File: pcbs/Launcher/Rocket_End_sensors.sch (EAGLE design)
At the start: 7 parts, among them U1 ARDUINO-MEGAPRO-5V, X1 22-23-2051, X3 22-23-2041, X5 22-23-2101, X6 22-23-2101

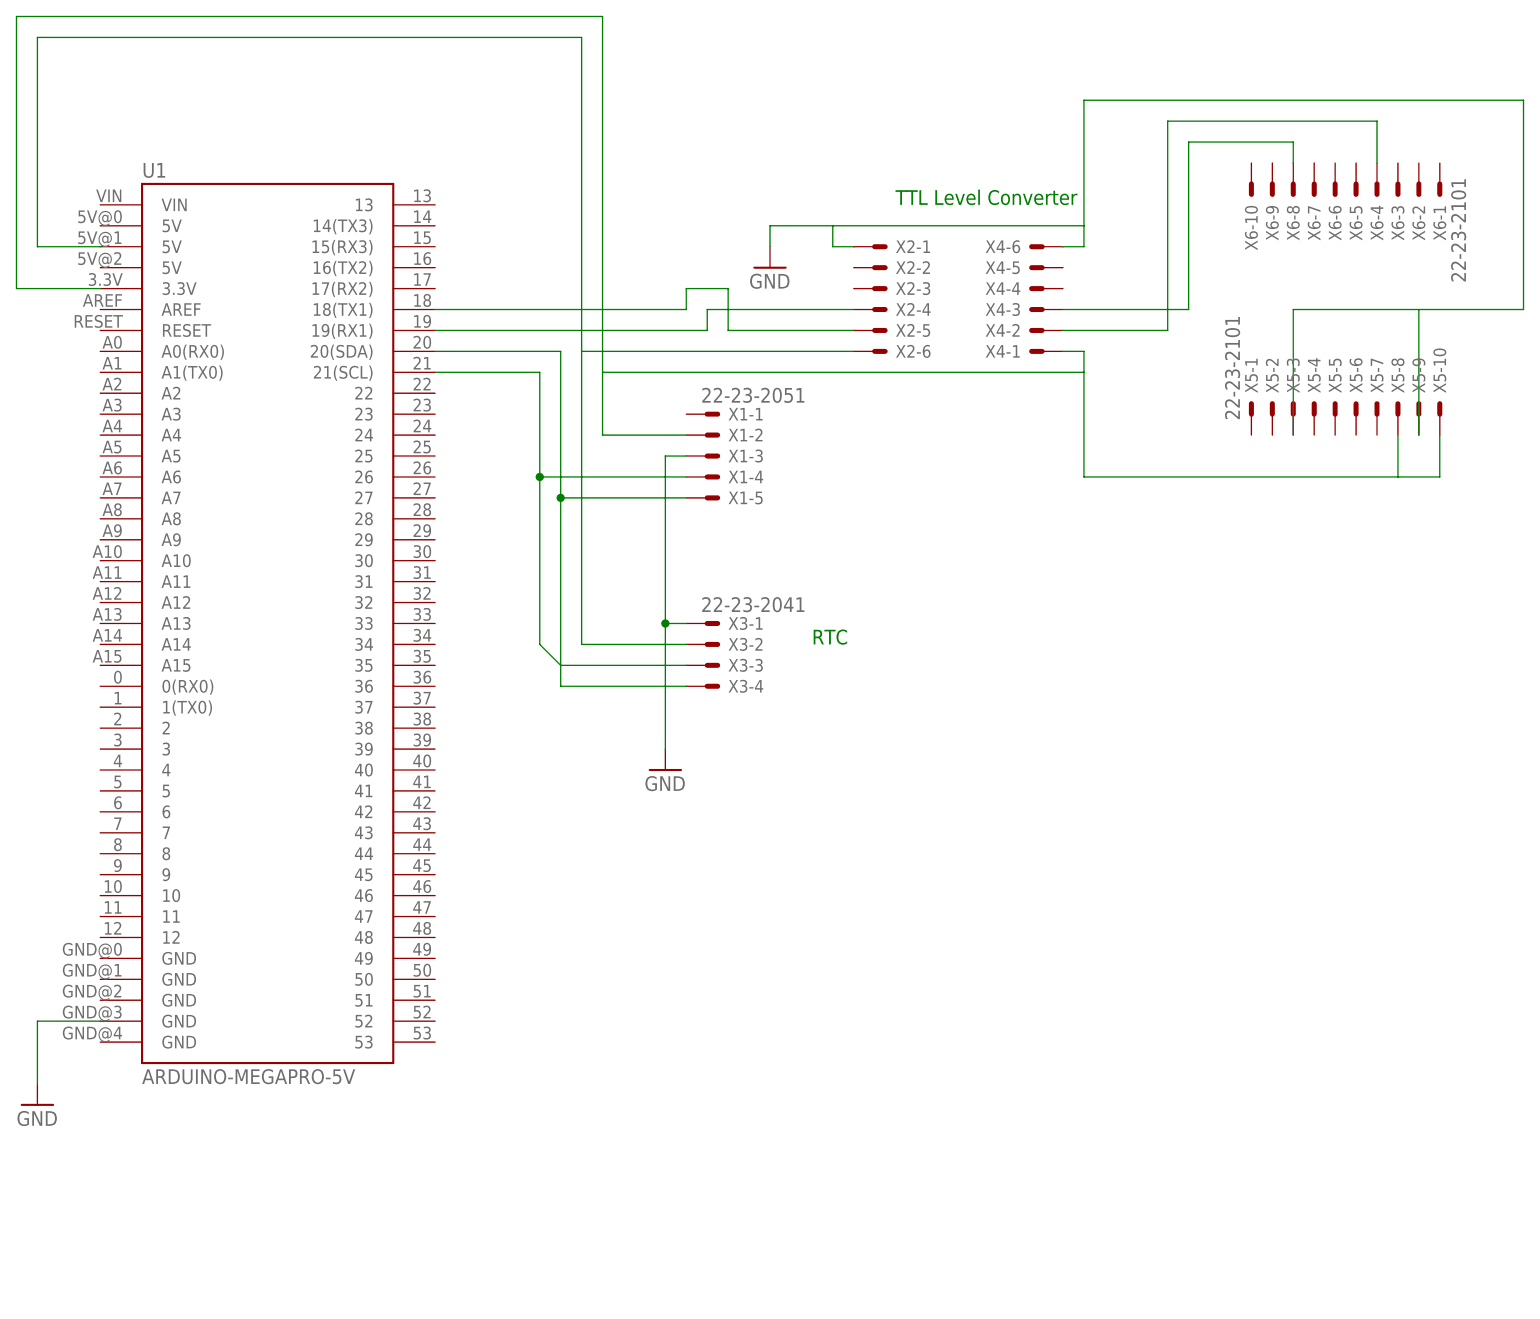
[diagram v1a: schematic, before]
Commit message: * Much better placement of components and tracks for Rocket_End * Put IMU on bottom of the Sensor board
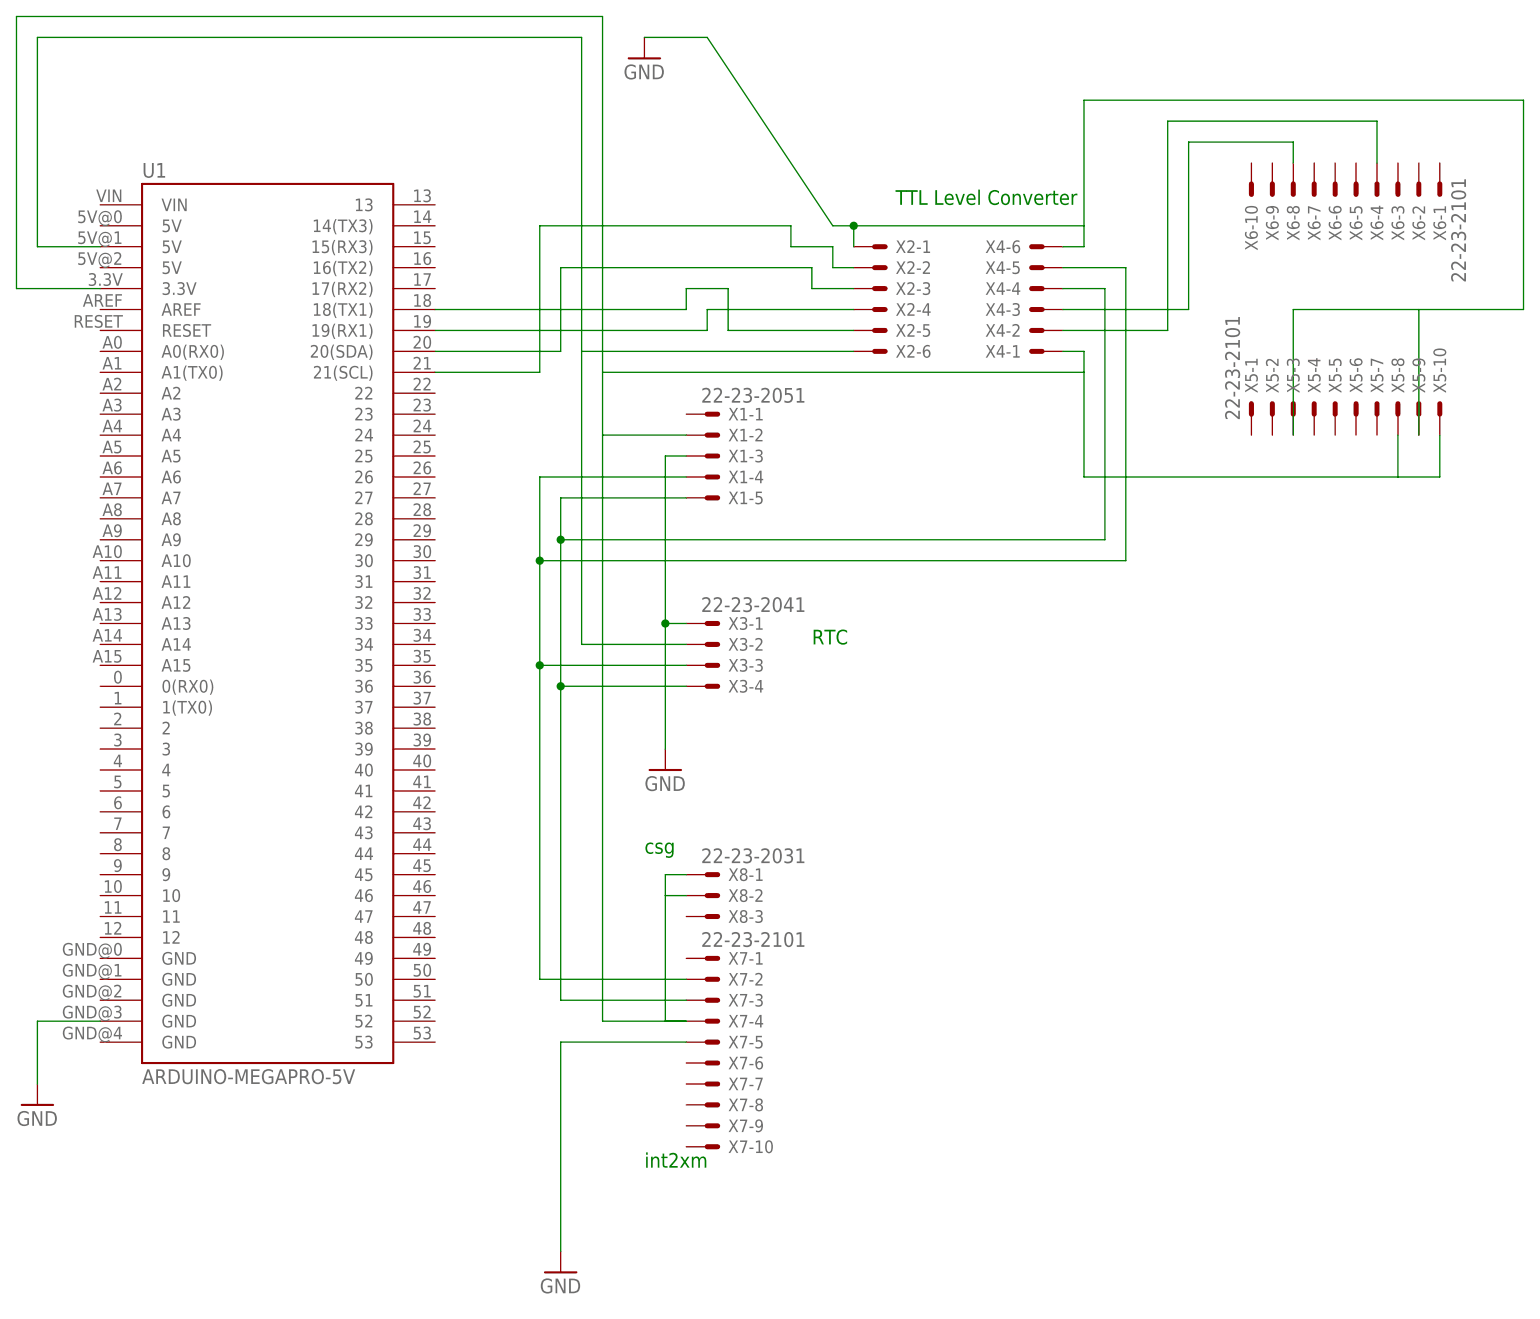
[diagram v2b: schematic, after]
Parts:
- added X7: 22-23-2101, con-molex:22-23-2101
- added X8: 22-23-2031, con-molex:22-23-2031
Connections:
- new net N$2: U1.21(SCL), X2-2.S
- new net N$5: U1.20(SDA), X2-3.S
- new net N$7: X2-1.S, X4-6.S, X5-3.S, X5-9.S
- net GND: now also X7-5.S; no longer X2-1.S, X4-6.S, X5-3.S, X5-9.S
- net N$18: now also X4-4.S, X7-3.S; no longer U1.20(SDA)
- net N$24: now also X4-5.S, X7-2.S; no longer U1.21(SCL)
- net N$4: now also X7-4.S, X8-1.S, X8-2.S
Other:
- note added: "csg"
- note added: "int2xm"
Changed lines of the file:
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@@
 <part name="X5" library="con-molex" deviceset="22-23-2101" device=""/>
 <part name="X6" library="con-molex" deviceset="22-23-2101" device=""/>
+<part name="X7" library="con-molex" deviceset="22-23-2101" device=""/>
+<part name="X8" library="con-molex" deviceset="22-23-2031" device=""/>
+<part name="GND3" library="supply1" deviceset="GND" device=""/>
 </parts>
 <sheets>
@@
 <text x="104.14" y="50.8" size="1.778" layer="91">RTC</text>
 <text x="114.3" y="104.14" size="1.778" layer="91">TTL Level Converter</text>
+<text x="83.82" y="-12.7" size="1.778" layer="91">int2xm</text>
+<text x="83.82" y="25.4" size="1.778" layer="91">csg</text>
 </plain>
 <instances>
@@
 <instance part="X4" gate="-5" x="132.08" y="96.52" rot="R180"/>
 <instance part="X4" gate="-6" x="132.08" y="99.06" rot="R180"/>
-<instance part="GND2" gate="1" x="99.06" y="96.52"/>
+<instance part="GND2" gate="1" x="83.82" y="121.92"/>
 <instance part="X5" gate="-1" x="157.48" y="78.74" rot="R90"/>
 <instance part="X5" gate="-2" x="160.02" y="78.74" rot="R90"/>
@@
 <instance part="X6" gate="-9" x="160.02" y="106.68" rot="R270"/>
 <instance part="X6" gate="-10" x="157.48" y="106.68" rot="R270"/>
+<instance part="X7" gate="-1" x="91.44" y="12.7"/>
+<instance part="X7" gate="-2" x="91.44" y="10.16"/>
+<instance part="X7" gate="-3" x="91.44" y="7.62"/>
+<instance part="X7" gate="-4" x="91.44" y="5.08"/>
+<instance part="X7" gate="-5" x="91.44" y="2.54"/>
+<instance part="X7" gate="-6" x="91.44" y="0"/>
+<instance part="X7" gate="-7" x="91.44" y="-2.54"/>
+<instance part="X7" gate="-8" x="91.44" y="-5.08"/>
+<instance part="X7" gate="-9" x="91.44" y="-7.62"/>
+<instance part="X7" gate="-10" x="91.44" y="-10.16"/>
+<instance part="X8" gate="-1" x="91.44" y="22.86"/>
+<instance part="X8" gate="-2" x="91.44" y="20.32"/>
+<instance part="X8" gate="-3" x="91.44" y="17.78"/>
+<instance part="GND3" gate="1" x="73.66" y="-25.4"/>
 </instances>
 <busses>
@@
 </segment>
 <segment>
-<pinref part="X4" gate="-6" pin="S"/>
-<wire x1="134.62" y1="99.06" x2="137.16" y2="99.06" width="0.1524" layer="91"/>
-<wire x1="137.16" y1="99.06" x2="137.16" y2="101.6" width="0.1524" layer="91"/>
-<wire x1="137.16" y1="101.6" x2="106.68" y2="101.6" width="0.1524" layer="91"/>
-<wire x1="106.68" y1="101.6" x2="106.68" y2="99.06" width="0.1524" layer="91"/>
-<pinref part="X2" gate="-1" pin="S"/>
-<wire x1="106.68" y1="99.06" x2="109.22" y2="99.06" width="0.1524" layer="91"/>
-<wire x1="106.68" y1="101.6" x2="99.06" y2="101.6" width="0.1524" layer="91"/>
-<wire x1="99.06" y1="101.6" x2="99.06" y2="99.06" width="0.1524" layer="91"/>
+<wire x1="106.68" y1="101.6" x2="91.44" y2="124.46" width="0.1524" layer="91"/>
+<wire x1="91.44" y1="124.46" x2="83.82" y2="124.46" width="0.1524" layer="91"/>
 <pinref part="GND2" gate="1" pin="GND"/>
-<pinref part="X5" gate="-9" pin="S"/>
-<wire x1="177.8" y1="76.2" x2="177.8" y2="91.44" width="0.1524" layer="91"/>
-<wire x1="177.8" y1="91.44" x2="162.56" y2="91.44" width="0.1524" layer="91"/>
-<pinref part="X5" gate="-3" pin="S"/>
-<wire x1="162.56" y1="91.44" x2="162.56" y2="76.2" width="0.1524" layer="91"/>
-<wire x1="177.8" y1="91.44" x2="190.5" y2="91.44" width="0.1524" layer="91"/>
-<wire x1="190.5" y1="91.44" x2="190.5" y2="116.84" width="0.1524" layer="91"/>
-<wire x1="190.5" y1="116.84" x2="137.16" y2="116.84" width="0.1524" layer="91"/>
-<wire x1="137.16" y1="116.84" x2="137.16" y2="101.6" width="0.1524" layer="91"/>
+</segment>
+<segment>
+<pinref part="X7" gate="-5" pin="S"/>
+<wire x1="88.9" y1="2.54" x2="73.66" y2="2.54" width="0.1524" layer="91"/>
+<wire x1="73.66" y1="2.54" x2="73.66" y2="-22.86" width="0.1524" layer="91"/>
+<pinref part="GND3" gate="1" pin="GND"/>
 </segment>
 </net>
 <net name="N$18" class="0">
 <segment>
-<pinref part="U1" gate="G$1" pin="20(SDA)"/>
-<wire x1="58.42" y1="86.36" x2="73.66" y2="86.36" width="0.1524" layer="91"/>
-<wire x1="73.66" y1="86.36" x2="73.66" y2="68.58" width="0.1524" layer="91"/>
-<pinref part="X3" gate="-4" pin="S"/>
-<wire x1="73.66" y1="68.58" x2="73.66" y2="45.72" width="0.1524" layer="91"/>
-<wire x1="73.66" y1="45.72" x2="88.9" y2="45.72" width="0.1524" layer="91"/>
+<wire x1="73.66" y1="68.58" x2="73.66" y2="63.5" width="0.1524" layer="91"/>
 <pinref part="X1" gate="-5" pin="S"/>
 <wire x1="88.9" y1="68.58" x2="73.66" y2="68.58" width="0.1524" layer="91"/>
-<junction x="73.66" y="68.58"/>
+<pinref part="X7" gate="-3" pin="S"/>
+<wire x1="73.66" y1="63.5" x2="73.66" y2="45.72" width="0.1524" layer="91"/>
+<wire x1="73.66" y1="45.72" x2="73.66" y2="7.62" width="0.1524" layer="91"/>
+<wire x1="73.66" y1="7.62" x2="88.9" y2="7.62" width="0.1524" layer="91"/>
+<wire x1="73.66" y1="63.5" x2="139.7" y2="63.5" width="0.1524" layer="91"/>
+<wire x1="139.7" y1="63.5" x2="139.7" y2="93.98" width="0.1524" layer="91"/>
+<pinref part="X4" gate="-4" pin="S"/>
+<wire x1="139.7" y1="93.98" x2="134.62" y2="93.98" width="0.1524" layer="91"/>
+<junction x="73.66" y="63.5"/>
+<pinref part="X3" gate="-4" pin="S"/>
+<wire x1="88.9" y1="45.72" x2="73.66" y2="45.72" width="0.1524" layer="91"/>
+<junction x="73.66" y="45.72"/>
 </segment>
 </net>
 <net name="N$24" class="0">
 <segment>
-<pinref part="U1" gate="G$1" pin="21(SCL)"/>
-<wire x1="58.42" y1="83.82" x2="71.12" y2="83.82" width="0.1524" layer="91"/>
-<wire x1="71.12" y1="83.82" x2="71.12" y2="71.12" width="0.1524" layer="91"/>
-<pinref part="X3" gate="-3" pin="S"/>
-<wire x1="71.12" y1="71.12" x2="71.12" y2="50.8" width="0.1524" layer="91"/>
-<wire x1="71.12" y1="50.8" x2="73.66" y2="48.26" width="0.1524" layer="91"/>
-<wire x1="73.66" y1="48.26" x2="88.9" y2="48.26" width="0.1524" layer="91"/>
+<wire x1="71.12" y1="71.12" x2="71.12" y2="60.96" width="0.1524" layer="91"/>
 <pinref part="X1" gate="-4" pin="S"/>
 <wire x1="88.9" y1="71.12" x2="71.12" y2="71.12" width="0.1524" layer="91"/>
-<junction x="71.12" y="71.12"/>
+<pinref part="X7" gate="-2" pin="S"/>
+<wire x1="71.12" y1="60.96" x2="71.12" y2="48.26" width="0.1524" layer="91"/>
+<wire x1="71.12" y1="48.26" x2="71.12" y2="10.16" width="0.1524" layer="91"/>
+<wire x1="71.12" y1="10.16" x2="88.9" y2="10.16" width="0.1524" layer="91"/>
+<pinref part="X4" gate="-5" pin="S"/>
+<wire x1="134.62" y1="96.52" x2="142.24" y2="96.52" width="0.1524" layer="91"/>
+<wire x1="142.24" y1="96.52" x2="142.24" y2="60.96" width="0.1524" layer="91"/>
+<wire x1="142.24" y1="60.96" x2="71.12" y2="60.96" width="0.1524" layer="91"/>
+<junction x="71.12" y="60.96"/>
+<pinref part="X3" gate="-3" pin="S"/>
+<wire x1="88.9" y1="48.26" x2="71.12" y2="48.26" width="0.1524" layer="91"/>
+<junction x="71.12" y="48.26"/>
 </segment>
 </net>
@@
 <wire x1="175.26" y1="71.12" x2="137.16" y2="71.12" width="0.1524" layer="91"/>
 <wire x1="137.16" y1="71.12" x2="137.16" y2="83.82" width="0.1524" layer="91"/>
+<wire x1="78.74" y1="76.2" x2="78.74" y2="5.08" width="0.1524" layer="91"/>
+<pinref part="X7" gate="-4" pin="S"/>
+<wire x1="78.74" y1="5.08" x2="88.9" y2="5.08" width="0.1524" layer="91"/>
+<wire x1="88.9" y1="5.08" x2="86.36" y2="5.08" width="0.1524" layer="91"/>
+<wire x1="86.36" y1="5.08" x2="86.36" y2="20.32" width="0.1524" layer="91"/>
+<pinref part="X8" gate="-1" pin="S"/>
+<wire x1="86.36" y1="20.32" x2="86.36" y2="22.86" width="0.1524" layer="91"/>
+<wire x1="86.36" y1="22.86" x2="88.9" y2="22.86" width="0.1524" layer="91"/>
+<pinref part="X8" gate="-2" pin="S"/>
+<wire x1="88.9" y1="20.32" x2="86.36" y2="20.32" width="0.1524" layer="91"/>
 </segment>
 </net>
@@
 </segment>
 </net>
+<net name="N$2" class="0">
+<segment>
+<pinref part="U1" gate="G$1" pin="21(SCL)"/>
+<wire x1="58.42" y1="83.82" x2="71.12" y2="83.82" width="0.1524" layer="91"/>
+<wire x1="71.12" y1="83.82" x2="71.12" y2="101.6" width="0.1524" layer="91"/>
+<wire x1="71.12" y1="101.6" x2="101.6" y2="101.6" width="0.1524" layer="91"/>
+<wire x1="101.6" y1="101.6" x2="101.6" y2="99.06" width="0.1524" layer="91"/>
+<wire x1="101.6" y1="99.06" x2="106.68" y2="99.06" width="0.1524" layer="91"/>
+<wire x1="106.68" y1="99.06" x2="106.68" y2="96.52" width="0.1524" layer="91"/>
+<pinref part="X2" gate="-2" pin="S"/>
+<wire x1="106.68" y1="96.52" x2="109.22" y2="96.52" width="0.1524" layer="91"/>
+</segment>
+</net>
+<net name="N$5" class="0">
+<segment>
+<pinref part="U1" gate="G$1" pin="20(SDA)"/>
+<wire x1="58.42" y1="86.36" x2="73.66" y2="86.36" width="0.1524" layer="91"/>
+<pinref part="X2" gate="-3" pin="S"/>
+<wire x1="109.22" y1="93.98" x2="104.14" y2="93.98" width="0.1524" layer="91"/>
+<wire x1="104.14" y1="93.98" x2="104.14" y2="96.52" width="0.1524" layer="91"/>
+<wire x1="104.14" y1="96.52" x2="73.66" y2="96.52" width="0.1524" layer="91"/>
+<wire x1="73.66" y1="96.52" x2="73.66" y2="86.36" width="0.1524" layer="91"/>
+</segment>
+</net>
+<net name="N$7" class="0">
+<segment>
+<pinref part="X4" gate="-6" pin="S"/>
+<wire x1="134.62" y1="99.06" x2="137.16" y2="99.06" width="0.1524" layer="91"/>
+<wire x1="137.16" y1="99.06" x2="137.16" y2="101.6" width="0.1524" layer="91"/>
+<wire x1="137.16" y1="101.6" x2="109.22" y2="101.6" width="0.1524" layer="91"/>
+<pinref part="X2" gate="-1" pin="S"/>
+<pinref part="X5" gate="-9" pin="S"/>
+<wire x1="177.8" y1="76.2" x2="177.8" y2="91.44" width="0.1524" layer="91"/>
+<wire x1="177.8" y1="91.44" x2="162.56" y2="91.44" width="0.1524" layer="91"/>
+<pinref part="X5" gate="-3" pin="S"/>
+<wire x1="162.56" y1="91.44" x2="162.56" y2="76.2" width="0.1524" layer="91"/>
+<wire x1="177.8" y1="91.44" x2="190.5" y2="91.44" width="0.1524" layer="91"/>
+<wire x1="190.5" y1="91.44" x2="190.5" y2="116.84" width="0.1524" layer="91"/>
+<wire x1="190.5" y1="116.84" x2="137.16" y2="116.84" width="0.1524" layer="91"/>
+<wire x1="137.16" y1="116.84" x2="137.16" y2="101.6" width="0.1524" layer="91"/>
+<wire x1="109.22" y1="99.06" x2="109.22" y2="101.6" width="0.1524" layer="91"/>
+<wire x1="109.22" y1="101.6" x2="106.68" y2="101.6" width="0.1524" layer="91"/>
+<junction x="109.22" y="101.6"/>
+</segment>
+</net>
